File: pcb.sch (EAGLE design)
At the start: 138 parts

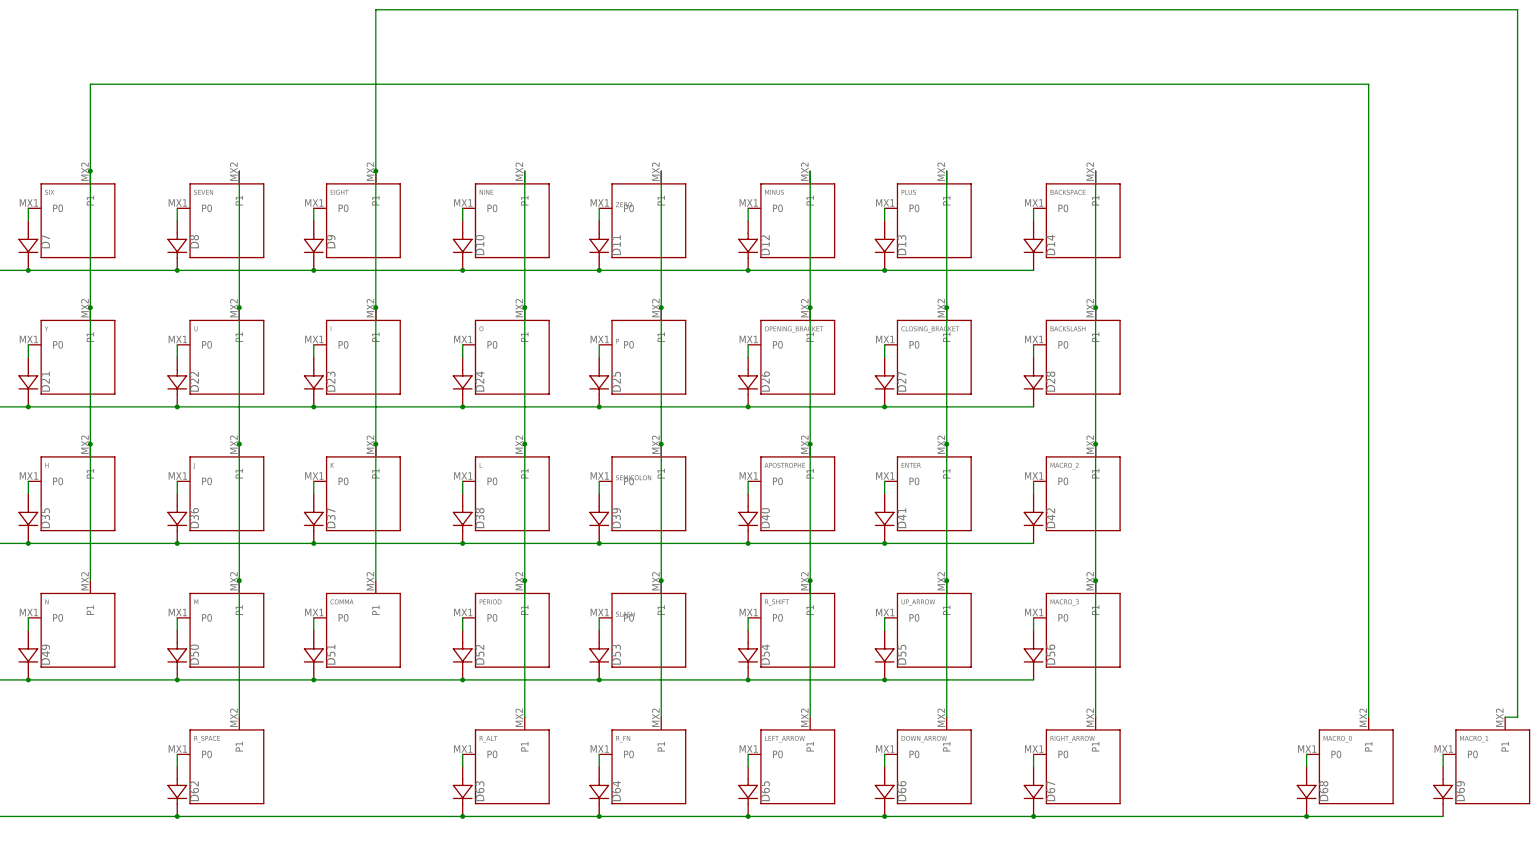
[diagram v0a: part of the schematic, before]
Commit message: updated matrix and streched pcb
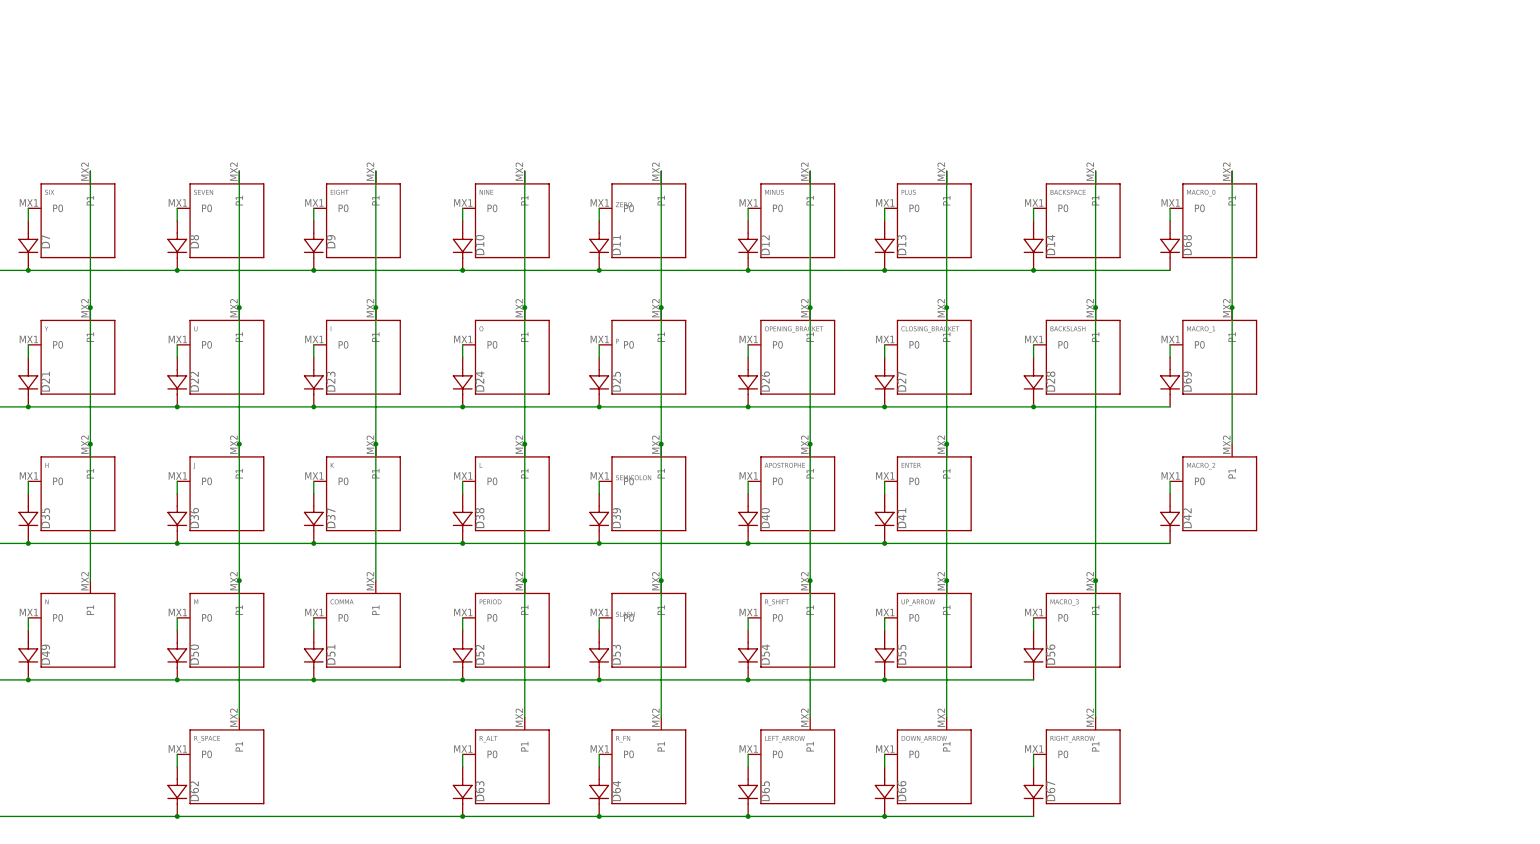
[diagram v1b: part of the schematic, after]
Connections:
- new net N$84: MACRO_0.P1, MACRO_1.P1, MACRO_2.P1
- net N$76: no longer MACRO_0.P1
- net N$78: no longer MACRO_1.P1
- net N$83: no longer MACRO_2.P1
- net ROW0: now also D68.C
- net ROW1: now also D69.C
- net ROW4: no longer D68.C, D69.C
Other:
- moved on the sheet: D42, D68, D69, MACRO_0, MACRO_1, MACRO_2
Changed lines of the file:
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@@
 <attribute name="NAME" x="343.71" y="-12.462" size="1" layer="95"/>
 </instance>
-<instance part="MACRO_2" gate="G$1" x="408.94" y="-17.78" smashed="yes">
-<attribute name="NAME" x="402.13" y="-12.462" size="1" layer="95"/>
+<instance part="MACRO_2" gate="G$1" x="436.88" y="-17.78" smashed="yes">
+<attribute name="NAME" x="430.07" y="-12.462" size="1" layer="95"/>
 </instance>
 <instance part="Z" gate="G$1" x="58.42" y="-45.72" smashed="yes">
@@
 <attribute name="NAME" x="402.13" y="-68.342" size="1" layer="95"/>
 </instance>
-<instance part="MACRO_0" gate="G$1" x="464.82" y="-73.66" smashed="yes">
-<attribute name="NAME" x="458.01" y="-68.342" size="1" layer="95"/>
-</instance>
-<instance part="MACRO_1" gate="G$1" x="492.76" y="-73.66" smashed="yes">
-<attribute name="NAME" x="485.95" y="-68.342" size="1" layer="95"/>
+<instance part="MACRO_0" gate="G$1" x="436.88" y="38.1" smashed="yes">
+<attribute name="NAME" x="430.07" y="43.418" size="1" layer="95"/>
+</instance>
+<instance part="MACRO_1" gate="G$1" x="436.88" y="10.16" smashed="yes">
+<attribute name="NAME" x="430.07" y="15.478" size="1" layer="95"/>
 </instance>
 <instance part="L_SPACE" gate="G$1" x="144.78" y="-73.66" smashed="yes">
@@
 <attribute name="VALUE" x="363.8042" y="-20.2946" size="1.778" layer="96" rot="R270"/>
 </instance>
-<instance part="D42" gate="D$1" x="398.78" y="-22.86" smashed="yes" rot="R270">
-<attribute name="NAME" x="401.4216" y="-20.5486" size="1.778" layer="95" rot="R270"/>
-<attribute name="VALUE" x="394.2842" y="-20.2946" size="1.778" layer="96" rot="R270"/>
+<instance part="D42" gate="D$1" x="426.72" y="-22.86" smashed="yes" rot="R270">
+<attribute name="NAME" x="429.3616" y="-20.5486" size="1.778" layer="95" rot="R270"/>
+<attribute name="VALUE" x="422.2242" y="-20.2946" size="1.778" layer="96" rot="R270"/>
 </instance>
 <instance part="D43" gate="D$1" x="17.78" y="-50.8" smashed="yes" rot="R270">
@@
 <attribute name="VALUE" x="160.6042" y="-76.1746" size="1.778" layer="96" rot="R270"/>
 </instance>
-<instance part="D68" gate="D$1" x="454.66" y="-78.74" smashed="yes" rot="R270">
-<attribute name="NAME" x="457.3016" y="-76.4286" size="1.778" layer="95" rot="R270"/>
-<attribute name="VALUE" x="450.1642" y="-76.1746" size="1.778" layer="96" rot="R270"/>
+<instance part="D68" gate="D$1" x="426.72" y="33.02" smashed="yes" rot="R270">
+<attribute name="NAME" x="429.3616" y="35.3314" size="1.778" layer="95" rot="R270"/>
+<attribute name="VALUE" x="422.2242" y="35.5854" size="1.778" layer="96" rot="R270"/>
 </instance>
 <instance part="D62" gate="D$1" x="223.52" y="-78.74" smashed="yes" rot="R270">
@@
 <attribute name="VALUE" x="219.0242" y="-76.1746" size="1.778" layer="96" rot="R270"/>
 </instance>
-<instance part="D69" gate="D$1" x="482.6" y="-78.74" smashed="yes" rot="R270">
-<attribute name="NAME" x="485.2416" y="-76.4286" size="1.778" layer="95" rot="R270"/>
-<attribute name="VALUE" x="478.1042" y="-76.1746" size="1.778" layer="96" rot="R270"/>
+<instance part="D69" gate="D$1" x="426.72" y="5.08" smashed="yes" rot="R270">
+<attribute name="NAME" x="429.3616" y="7.3914" size="1.778" layer="95" rot="R270"/>
+<attribute name="VALUE" x="422.2242" y="7.6454" size="1.778" layer="96" rot="R270"/>
 </instance>
 <instance part="D63" gate="D$1" x="281.94" y="-78.74" smashed="yes" rot="R270">
@@
 </segment>
 </net>
-<net name="N$42" class="0">
-<segment>
-<pinref part="MACRO_2" gate="G$1" pin="P0"/>
-<pinref part="D42" gate="D$1" pin="A"/>
-<wire x1="398.78" y1="-17.78" x2="398.78" y2="-15.24" width="0.1524" layer="91"/>
-</segment>
-</net>
 <net name="N$43" class="0">
 <segment>
@@
 <pinref part="MACRO_1" gate="G$1" pin="P0"/>
 <pinref part="D69" gate="D$1" pin="A"/>
-<wire x1="482.6" y1="-73.66" x2="482.6" y2="-71.12" width="0.1524" layer="91"/>
+<wire x1="426.72" y1="10.16" x2="426.72" y2="12.7" width="0.1524" layer="91"/>
 </segment>
 </net>
@@
 <pinref part="MACRO_0" gate="G$1" pin="P0"/>
 <pinref part="D68" gate="D$1" pin="A"/>
-<wire x1="454.66" y1="-73.66" x2="454.66" y2="-71.12" width="0.1524" layer="91"/>
+<wire x1="426.72" y1="38.1" x2="426.72" y2="40.64" width="0.1524" layer="91"/>
 </segment>
 </net>
@@
 <junction x="17.78" y="0"/>
 <label x="0" y="-2.54" size="1.778" layer="95"/>
+<pinref part="D69" gate="D$1" pin="C"/>
+<wire x1="398.78" y1="0" x2="426.72" y2="0" width="0.1524" layer="91"/>
+<junction x="398.78" y="0"/>
 </segment>
 </net>
@@
 <segment>
 <pinref part="D29" gate="D$1" pin="C"/>
-<pinref part="D42" gate="D$1" pin="C"/>
 <wire x1="17.78" y1="-27.94" x2="48.26" y2="-27.94" width="0.1524" layer="91"/>
 <pinref part="D30" gate="D$1" pin="C"/>
@@
 <junction x="340.36" y="-27.94"/>
 <pinref part="D41" gate="D$1" pin="C"/>
-<wire x1="368.3" y1="-27.94" x2="398.78" y2="-27.94" width="0.1524" layer="91"/>
-<junction x="368.3" y="-27.94"/>
 <wire x1="17.78" y1="-27.94" x2="0" y2="-27.94" width="0.1524" layer="91"/>
 <junction x="17.78" y="-27.94"/>
 <label x="0" y="-30.48" size="1.778" layer="95"/>
+<pinref part="D42" gate="D$1" pin="C"/>
+<wire x1="368.3" y1="-27.94" x2="426.72" y2="-27.94" width="0.1524" layer="91"/>
+<junction x="368.3" y="-27.94"/>
 </segment>
 </net>
@@
 <segment>
 <pinref part="D57" gate="D$1" pin="C"/>
-<pinref part="D69" gate="D$1" pin="C"/>
 <wire x1="17.78" y1="-83.82" x2="48.26" y2="-83.82" width="0.1524" layer="91"/>
 <pinref part="D58" gate="D$1" pin="C"/>
@@
 <wire x1="165.1" y1="-83.82" x2="223.52" y2="-83.82" width="0.1524" layer="91"/>
 <junction x="165.1" y="-83.82"/>
-<pinref part="D68" gate="D$1" pin="C"/>
 <wire x1="223.52" y1="-83.82" x2="281.94" y2="-83.82" width="0.1524" layer="91"/>
 <wire x1="281.94" y1="-83.82" x2="309.88" y2="-83.82" width="0.1524" layer="91"/>
@@
 <wire x1="340.36" y1="-83.82" x2="368.3" y2="-83.82" width="0.1524" layer="91"/>
 <wire x1="368.3" y1="-83.82" x2="398.78" y2="-83.82" width="0.1524" layer="91"/>
-<wire x1="398.78" y1="-83.82" x2="454.66" y2="-83.82" width="0.1524" layer="91"/>
-<wire x1="454.66" y1="-83.82" x2="482.6" y2="-83.82" width="0.1524" layer="91"/>
-<junction x="454.66" y="-83.82"/>
 <pinref part="D62" gate="D$1" pin="C"/>
 <junction x="223.52" y="-83.82"/>
@@
 <junction x="340.36" y="-83.82"/>
 <pinref part="D67" gate="D$1" pin="C"/>
-<junction x="398.78" y="-83.82"/>
 <pinref part="D66" gate="D$1" pin="C"/>
 <junction x="368.3" y="-83.82"/>
@@
 <junction x="17.78" y="27.94"/>
 <label x="0" y="25.4" size="1.778" layer="95"/>
+<pinref part="D68" gate="D$1" pin="C"/>
+<wire x1="398.78" y1="27.94" x2="426.72" y2="27.94" width="0.1524" layer="91"/>
+<junction x="398.78" y="27.94"/>
 </segment>
 </net>
@@
 <net name="N$76" class="0">
 <segment>
-<pinref part="MACRO_0" gate="G$1" pin="P1"/>
-<wire x1="467.36" y1="-63.5" x2="467.36" y2="66.04" width="0.1524" layer="91"/>
 <pinref part="N" gate="G$1" pin="P1"/>
-<wire x1="467.36" y1="66.04" x2="205.74" y2="66.04" width="0.1524" layer="91"/>
-<wire x1="205.74" y1="66.04" x2="205.74" y2="48.26" width="0.1524" layer="91"/>
 <pinref part="SIX" gate="G$1" pin="P1"/>
 <wire x1="205.74" y1="48.26" x2="205.74" y2="20.32" width="0.1524" layer="91"/>
-<junction x="205.74" y="48.26"/>
 <pinref part="Y" gate="G$1" pin="P1"/>
 <wire x1="205.74" y1="20.32" x2="205.74" y2="-7.62" width="0.1524" layer="91"/>
@@
 <net name="N$78" class="0">
 <segment>
-<pinref part="MACRO_1" gate="G$1" pin="P1"/>
-<wire x1="495.3" y1="-63.5" x2="497.84" y2="-63.5" width="0.1524" layer="91"/>
-<wire x1="497.84" y1="-63.5" x2="497.84" y2="81.28" width="0.1524" layer="91"/>
-<wire x1="497.84" y1="81.28" x2="264.16" y2="81.28" width="0.1524" layer="91"/>
 <pinref part="COMMA" gate="G$1" pin="P1"/>
-<wire x1="264.16" y1="81.28" x2="264.16" y2="48.26" width="0.1524" layer="91"/>
 <pinref part="EIGHT" gate="G$1" pin="P1"/>
 <wire x1="264.16" y1="48.26" x2="264.16" y2="20.32" width="0.1524" layer="91"/>
-<junction x="264.16" y="48.26"/>
 <pinref part="I" gate="G$1" pin="P1"/>
 <wire x1="264.16" y1="20.32" x2="264.16" y2="-7.62" width="0.1524" layer="91"/>
@@
 </segment>
 </net>
+<net name="N$42" class="0">
+<segment>
+<pinref part="MACRO_2" gate="G$1" pin="P0"/>
+<pinref part="D42" gate="D$1" pin="A"/>
+<wire x1="426.72" y1="-15.24" x2="426.72" y2="-17.78" width="0.1524" layer="91"/>
+</segment>
+</net>
 <net name="N$83" class="0">
 <segment>
@@
 <wire x1="411.48" y1="48.26" x2="411.48" y2="20.32" width="0.1524" layer="91"/>
 <pinref part="BACKSLASH" gate="G$1" pin="P1"/>
-<wire x1="411.48" y1="20.32" x2="411.48" y2="-7.62" width="0.1524" layer="91"/>
+<wire x1="411.48" y1="20.32" x2="411.48" y2="-35.56" width="0.1524" layer="91"/>
 <junction x="411.48" y="20.32"/>
-<pinref part="MACRO_2" gate="G$1" pin="P1"/>
-<wire x1="411.48" y1="-7.62" x2="411.48" y2="-35.56" width="0.1524" layer="91"/>
-<junction x="411.48" y="-7.62"/>
 <pinref part="MACRO_3" gate="G$1" pin="P1"/>
 <wire x1="411.48" y1="-35.56" x2="411.48" y2="-63.5" width="0.1524" layer="91"/>
@@
 </segment>
 </net>
+<net name="N$84" class="0">
+<segment>
+<pinref part="MACRO_0" gate="G$1" pin="P1"/>
+<pinref part="MACRO_2" gate="G$1" pin="P1"/>
+<wire x1="439.42" y1="48.26" x2="439.42" y2="20.32" width="0.1524" layer="91"/>
+<pinref part="MACRO_1" gate="G$1" pin="P1"/>
+<wire x1="439.42" y1="20.32" x2="439.42" y2="-7.62" width="0.1524" layer="91"/>
+<junction x="439.42" y="20.32"/>
+</segment>
+</net>

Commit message: added MCU scheme + readme
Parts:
- added C1, C2, C3, C4: 0.1uF, Components:CAPACITOR-0603
- added C5: 10uF, Components:CAPACITOR-0603
- added C6: 1uF, Components:CAPACITOR-0603
- added C7, C8: 22pF, Components:CAPACITOR-0603
- added R1, R2: 22, Components:RESISTOR-0603
- added R3, R4: 10k, Components:RESISTOR-0603
- added SW1: SWITCH-SMD-EVP-BB2A9B00, Controller:SWITCH-SMD-EVP-BB2A9B00
- added U$1: ATMEGA32U4-QFN44, MCU:ATMEGA32U4-QFN44
- added Y1: 16MHz, SparkFun-Clocks:CRYSTAL-16MHZ_SMALL
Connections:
- new net D+: R2.1
- new net D-: R1.1
- new net GND: C1.1, C2.1, C3.1, C4.1, C5.1, C6.1, C7.1, C8.1, R4.1, SW1.1, U$1.GND@15, U$1.GND@23, U$1.GND@35, U$1.GND@43, U$1.UGND, Y1.GND
- new net N$85: R4.2, U$1.PE2(!HWB)
- new net N$86: R3.2, SW1.2, U$1.!RESET
- new net N$87: C7.2, U$1.XTAL1, Y1.1
- new net N$88: C8.2, U$1.XTAL2, Y1.2
- new net N$89: R2.2, U$1.D+
- new net N$90: R1.2, U$1.D-
- new net N$91: C6.2, U$1.UCAP
- new net VCC: C1.2, C2.2, C3.2, C4.2, C5.2, R3.1, U$1.AVCC@24, U$1.AVCC@44, U$1.UVCC, U$1.VBUS, U$1.VCC@14, U$1.VCC@34
- net N$73: now also L_SPACE.P1
- net N$74: no longer L_SPACE.P1
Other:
- moved on the sheet: D60, L_SPACE

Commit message: added USB-C + ferrite beads
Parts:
- added FB1, FB2, FB3, FB4, FB5, FB6: 50@100 MHz, Filter:FBCHIP-0603(1608-METRIC)
- added J1, J2, J3: TYPE-C-31-M-12, TYPE-C-31-M-12:TYPE-C-31-M-12
- added R10, R5, R6, R7, R8, R9: 5.1k, Components:RESISTOR-0603
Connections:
- new net +5V: FB1.2, FB2.2, FB4.2
- new net N$100: FB6.1, J3.SHIELD
- new net N$92: J2.CC1, R7.1
- new net N$93: J1.CC1, R5.1
- new net N$94: J1.CC2, R6.1
- new net N$95: J2.CC2, R8.1
- new net N$96: FB5.1, J2.SHIELD
- new net N$97: J3.CC1, R9.1
- new net N$98: FB3.1, J1.SHIELD
- new net N$99: J3.CC2, R10.1
- new net VBUS: FB1.1, FB2.1, FB4.1, J1.VBUS, J2.VBUS, J3.VBUS
- net D+: now also J1.DP1, J1.DP2, J2.DP1, J2.DP2, J3.DP1, J3.DP2
- net D-: now also J1.DN1, J1.DN2, J2.DN1, J2.DN2, J3.DN1, J3.DN2
- net GND: now also FB3.2, FB5.2, FB6.2, J1.GND, J2.GND, J3.GND, R10.2, R5.2, R6.2, R7.2, R8.2, R9.2
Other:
- note added: "MCU"
- note added: "USB-C Connector"
- moved on the sheet: C1, C2, C3, C4
